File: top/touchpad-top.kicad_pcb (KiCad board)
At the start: 2 copper layers, 28.3 x 40 mm, 18 parts, among them P1 CONN_10, P2 CONN_5, U1 IQS572, U4 ESD

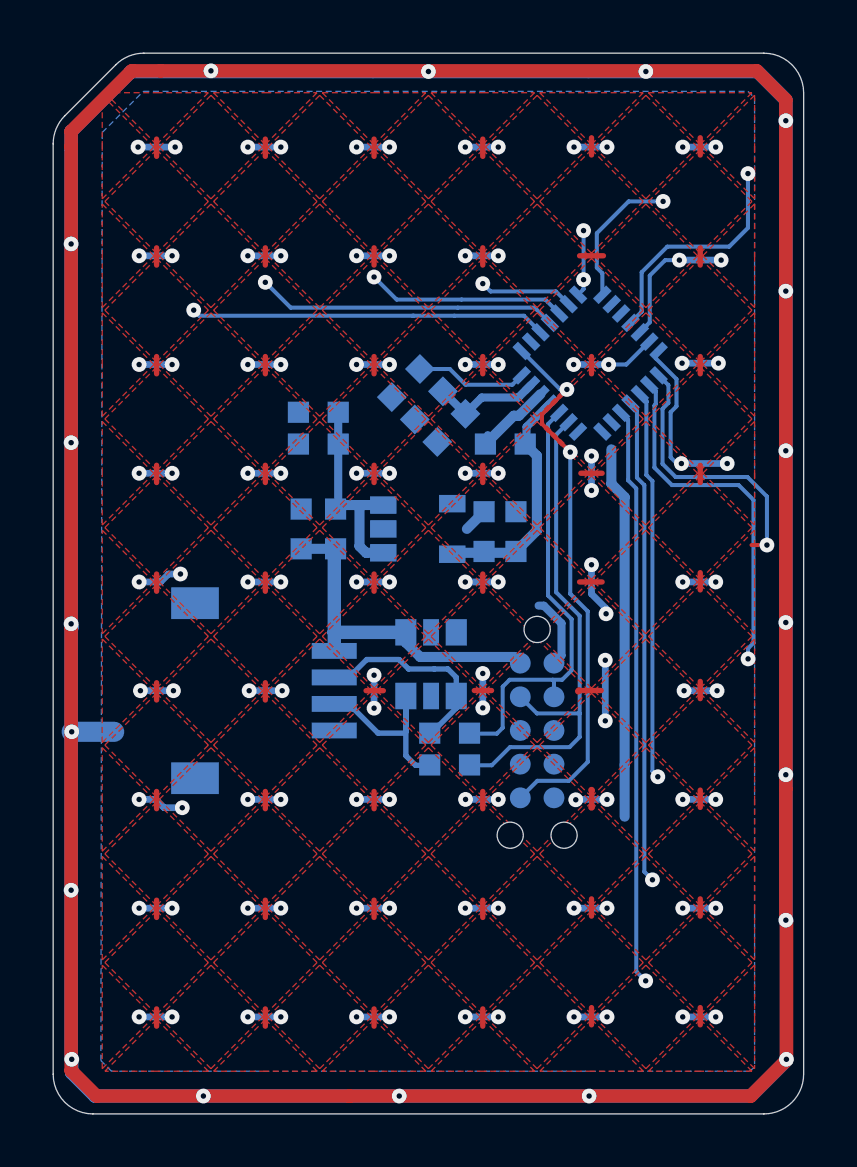
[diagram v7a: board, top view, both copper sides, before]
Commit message: Add GND island to sensors.
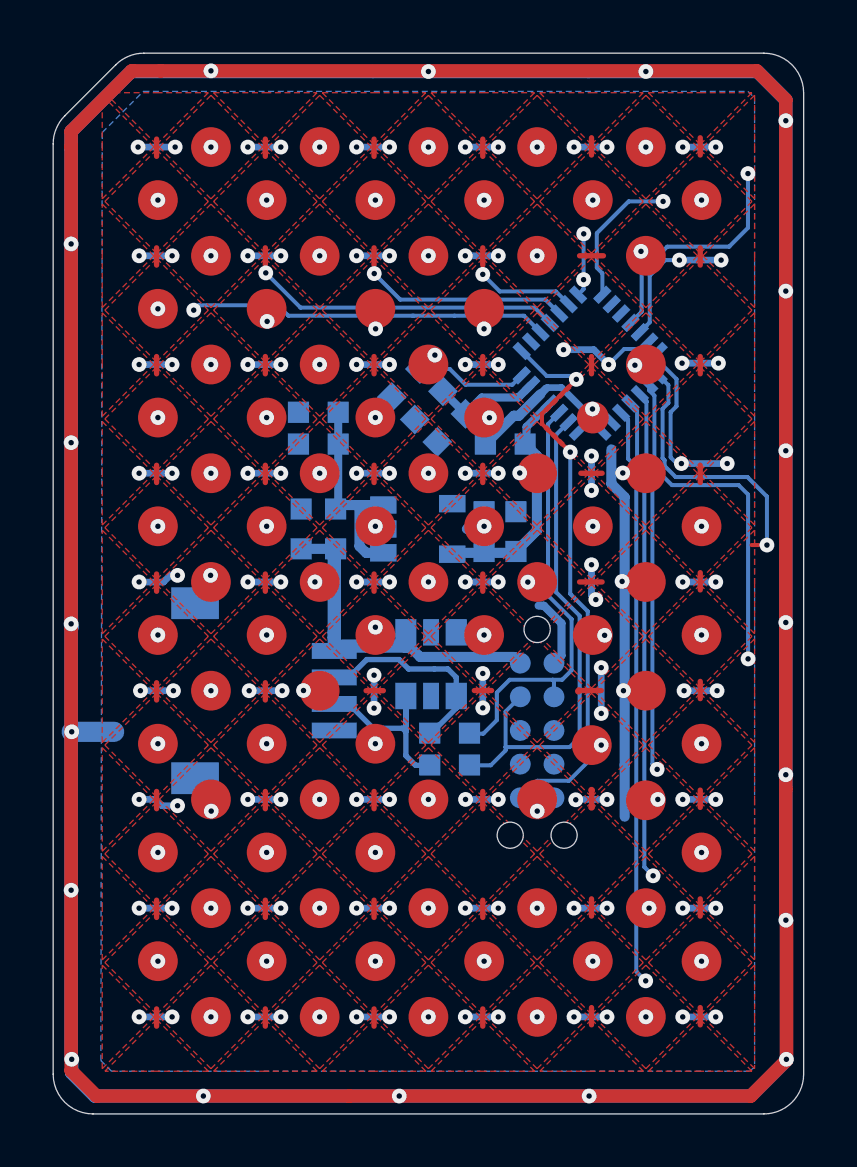
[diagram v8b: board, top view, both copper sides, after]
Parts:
- added pad: 1.5mm, UGL:smd_pad_1.2mm, F.Cu at (211.9, 132.2)
- added pad: 1.5mm, UGL:smd_pad_1.5mm, F.Cu at (199.6, 148.6)
- added pad: 1.5mm, UGL:smd_pad_1.5mm, F.Cu at (195.5, 148.6)
- added pad: 1.5mm, UGL:smd_pad_1.5mm, F.Cu at (216.0, 144.5)
- added pad: 1.5mm, UGL:smd_pad_1.5mm, F.Cu at (211.9, 144.6)
- added pad: 1.5mm, UGL:smd_pad_1.5mm, F.Cu at (203.7, 144.5)
- added pad: 1.5mm, UGL:smd_pad_1.5mm, F.Cu at (199.6, 144.5)
- added pad: 1.5mm, UGL:smd_pad_1.5mm, F.Cu at (195.5, 144.5)
- added pad: 1.5mm, UGL:smd_pad_1.5mm, F.Cu at (216.0, 140.4)
- added pad: 1.5mm, UGL:smd_pad_1.5mm, F.Cu at (211.9, 140.4)
- added pad: 1.5mm, UGL:smd_pad_1.5mm, F.Cu at (207.8, 140.4)
- added pad: 1.5mm, UGL:smd_pad_1.5mm, F.Cu at (216.0, 152.7)
- added pad: 1.5mm, UGL:smd_pad_1.5mm, F.Cu at (203.7, 140.4)
- added pad: 1.5mm, UGL:smd_pad_1.5mm, F.Cu at (199.6, 140.4)
- added pad: 1.5mm, UGL:smd_pad_1.5mm, F.Cu at (195.5, 140.4)
- added pad: 1.5mm, UGL:smd_pad_1.5mm, F.Cu at (216.0, 136.3)
- added pad: 1.5mm, UGL:smd_pad_1.5mm, F.Cu at (211.9, 136.3)
- added pad: 1.5mm, UGL:smd_pad_1.5mm, F.Cu at (207.8, 136.3)
- added pad: 1.5mm, UGL:smd_pad_1.5mm, F.Cu at (203.7, 136.3)
- added pad: 1.5mm, UGL:smd_pad_1.5mm, F.Cu at (199.6, 136.3)
- added pad: 1.5mm, UGL:smd_pad_1.5mm, F.Cu at (195.5, 136.3)
- added pad: 1.5mm, UGL:smd_pad_1.5mm, F.Cu at (207.8, 132.2)
- added pad: 1.5mm, UGL:smd_pad_1.5mm, F.Cu at (211.9, 152.7)
- added pad: 1.5mm, UGL:smd_pad_1.5mm, F.Cu at (203.7, 132.2)
- added pad: 1.5mm, UGL:smd_pad_1.5mm, F.Cu at (199.6, 132.2)
- added pad: 1.5mm, UGL:smd_pad_1.5mm, F.Cu at (195.5, 132.2)
- added pad: 1.5mm, UGL:smd_pad_1.5mm, F.Cu at (207.8, 128.1)
- added pad: 1.5mm, UGL:smd_pad_1.5mm, F.Cu at (203.7, 128.1)
- added pad: 1.5mm, UGL:smd_pad_1.5mm, F.Cu at (199.6, 128.1)
- added pad: 1.5mm, UGL:smd_pad_1.5mm, F.Cu at (195.5, 128.1)
- added pad: 1.5mm, UGL:smd_pad_1.5mm, F.Cu at (216.0, 124.0)
- added pad: 1.5mm, UGL:smd_pad_1.5mm, F.Cu at (211.9, 124.0)
- added pad: 1.5mm, UGL:smd_pad_1.5mm, F.Cu at (207.8, 124.0)
- added pad: 1.5mm, UGL:smd_pad_1.5mm, F.Cu at (207.8, 152.7)
- added pad: 1.5mm, UGL:smd_pad_1.5mm, F.Cu at (203.7, 124.0)
- added pad: 1.5mm, UGL:smd_pad_1.5mm, F.Cu at (199.6, 124.0)
- added pad: 1.5mm, UGL:smd_pad_1.5mm, F.Cu at (195.5, 124.0)
- added pad: 1.5mm, UGL:smd_pad_1.5mm, F.Cu at (213.9, 154.8)
- added pad: 1.5mm, UGL:smd_pad_1.5mm, F.Cu at (209.8, 154.8)
- added pad: 1.5mm, UGL:smd_pad_1.5mm, F.Cu at (205.7, 154.8)
- added pad: 1.5mm, UGL:smd_pad_1.5mm, F.Cu at (201.6, 154.8)
- added pad: 1.5mm, UGL:smd_pad_1.5mm, F.Cu at (197.5, 154.8)
- added pad: 1.5mm, UGL:smd_pad_1.5mm, F.Cu at (213.9, 150.7)
- added pad: 1.5mm, UGL:smd_pad_1.5mm, F.Cu at (209.8, 150.7)
- added pad: 1.5mm, UGL:smd_pad_1.5mm, F.Cu at (203.7, 152.7)
- added pad: 1.5mm, UGL:smd_pad_1.5mm, F.Cu at (205.7, 150.7)
- added pad: 1.5mm, UGL:smd_pad_1.5mm, F.Cu at (201.6, 150.7)
- added pad: 1.5mm, UGL:smd_pad_1.5mm, F.Cu at (197.5, 150.7)
- added pad: 1.5mm, UGL:smd_pad_1.5mm, F.Cu at (213.9, 146.6)
- added pad: 1.5mm, UGL:smd_pad_1.5mm, F.Cu at (209.8, 146.6)
- added pad: 1.5mm, UGL:smd_pad_1.5mm, F.Cu at (205.7, 146.6)
- added pad: 1.5mm, UGL:smd_pad_1.5mm, F.Cu at (201.6, 146.6)
- added pad: 1.5mm, UGL:smd_pad_1.5mm, F.Cu at (197.5, 146.6)
- added pad: 1.5mm, UGL:smd_pad_1.5mm, F.Cu at (213.9, 142.5)
- added pad: 1.5mm, UGL:smd_pad_1.5mm, F.Cu at (201.6, 142.5)
- added pad: 1.5mm, UGL:smd_pad_1.5mm, F.Cu at (199.6, 152.7)
- added pad: 1.5mm, UGL:smd_pad_1.5mm, F.Cu at (197.5, 142.5)
- added pad: 1.5mm, UGL:smd_pad_1.5mm, F.Cu at (213.9, 138.4)
- added pad: 1.5mm, UGL:smd_pad_1.5mm, F.Cu at (209.8, 138.4)
- added pad: 1.5mm, UGL:smd_pad_1.5mm, F.Cu at (205.7, 138.4)
- added pad: 1.5mm, UGL:smd_pad_1.5mm, F.Cu at (201.6, 138.4)
- added pad: 1.5mm, UGL:smd_pad_1.5mm, F.Cu at (197.5, 138.4)
- added pad: 1.5mm, UGL:smd_pad_1.5mm, F.Cu at (213.9, 134.3)
- added pad: 1.5mm, UGL:smd_pad_1.5mm, F.Cu at (209.8, 134.3)
- added pad: 1.5mm, UGL:smd_pad_1.5mm, F.Cu at (205.7, 134.3)
- added pad: 1.5mm, UGL:smd_pad_1.5mm, F.Cu at (201.6, 134.3)
- added pad: 1.5mm, UGL:smd_pad_1.5mm, F.Cu at (195.5, 152.7)
- added pad: 1.5mm, UGL:smd_pad_1.5mm, F.Cu at (197.5, 134.3)
- added pad: 1.5mm, UGL:smd_pad_1.5mm, F.Cu at (213.9, 130.2)
- added pad: 1.5mm, UGL:smd_pad_1.5mm, F.Cu at (205.7, 130.2)
- added pad: 1.5mm, UGL:smd_pad_1.5mm, F.Cu at (201.6, 130.2)
- added pad: 1.5mm, UGL:smd_pad_1.5mm, F.Cu at (197.5, 130.2)
- added pad: 1.5mm, UGL:smd_pad_1.5mm, F.Cu at (213.9, 126.1)
- added pad: 1.5mm, UGL:smd_pad_1.5mm, F.Cu at (209.8, 126.1)
- added pad: 1.5mm, UGL:smd_pad_1.5mm, F.Cu at (205.7, 126.1)
- added pad: 1.5mm, UGL:smd_pad_1.5mm, F.Cu at (201.6, 126.1)
- added pad: 1.5mm, UGL:smd_pad_1.5mm, F.Cu at (197.5, 126.1)
- added pad: 1.5mm, UGL:smd_pad_1.5mm, F.Cu at (216.0, 148.6)
- added pad: 1.5mm, UGL:smd_pad_1.5mm, F.Cu at (213.9, 122.0)
- added pad: 1.5mm, UGL:smd_pad_1.5mm, F.Cu at (209.8, 122.0)
- added pad: 1.5mm, UGL:smd_pad_1.5mm, F.Cu at (205.7, 122.0)
- added pad: 1.5mm, UGL:smd_pad_1.5mm, F.Cu at (201.6, 122.0)
- added pad: 1.5mm, UGL:smd_pad_1.5mm, F.Cu at (197.5, 122.0)
- added pad: 1.5mm, UGL:smd_pad_1.5mm, F.Cu at (203.7, 148.6)
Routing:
- net GND: track 278.3 -> 285.4 mm, vias 19 -> 103
- net /RX4: track 11.4 -> 10.1 mm
- net /RDY: track 20.6 -> 21.3 mm
- net /TX2: track 9.56 -> 10.2 mm
- net /TX6: track 22.6 -> 22.1 mm
